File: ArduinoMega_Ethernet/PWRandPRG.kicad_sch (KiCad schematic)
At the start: 98 parts, among them J1 RJ45_Amphenol_RJMG1BD3B8K1ANR, J11 Micro_SD_Card_Det_Hirose_DM3AT, J7 EXT_3V3_I2C, J9 PROGRAM_POWER_USBC, U10 TXS0108EPW, U2 CH340C, U3 ISM330DHCX, U4 W5500, U5 AP63205WU, U6 AP63203WU, U7 SE050C2HQ1, U8 AP22804AW5, U9 MCP7940N-xST, Y2 25Mhz, Y3 32.768kHz

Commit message: w6100 manufacturing and project files
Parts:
- removed C36: 10uF, Capacitor_SMD:C_0805_2012Metric_Pad1.18x1.45mm_HandSolder, symbol Device:C_Small
- removed D3, D5: LED, LED_SMD:LED_0603_1608Metric, symbol Device:LED
- removed J1: RJ45_Amphenol_RJMG1BD3B8K1ANR, Connector_RJ:RJ45_Amphenol_RJMG1BD3B8K1ANR, symbol Connector:RJ45_Amphenol_RJMG1BD3B8K1ANR
- removed JP1: PMODE1, Jumper:SolderJumper-3_P1.3mm_Bridged12_Pad1.0x1.5mm, symbol Jumper:SolderJumper_3_Bridged12
- removed JP2: PMODE0, Jumper:SolderJumper-3_P1.3mm_Bridged12_Pad1.0x1.5mm, symbol Jumper:SolderJumper_3_Bridged12
- removed JP3: PMODE2, Jumper:SolderJumper-3_P1.3mm_Bridged12_Pad1.0x1.5mm, symbol Jumper:SolderJumper_3_Bridged12
- removed R17, R19: 330R, Resistor_SMD:R_0603_1608Metric, symbol Device:R_Small_US
- removed R21: 12.4k, Resistor_SMD:R_0603_1608Metric, symbol Device:R_Small_US
- removed R22: 10R, Resistor_SMD:R_0603_1608Metric, symbol Device:R_Small_US
- removed R24, R26: 82R, Resistor_SMD:R_0603_1608Metric, symbol Device:R_Small_US
- removed U4: W5500, Package_QFP:LQFP-48_7x7mm_P0.5mm, symbol Interface_Ethernet:W5500
- added C50: 100nF, Capacitor_SMD:C_0603_1608Metric, symbol Device:C_Small
- added FB3, FB4: FerriteBead_Small, Inductor_SMD:L_0603_1608Metric, symbol Device:FerriteBead_Small
- added IC1: W6100L, EXT_ETHERNET:QFP50P900X900X160-48N, symbol EXT_ETHERNET:W6100L
- added P1: RB1-125BAG1A, EXT_ETHERNET:WIZNET_RB1-125BAG1A, symbol EXT_ETHERNET:RB1-125BAG1A
- added R33: 12.3k, Resistor_SMD:R_0603_1608Metric, symbol Device:R_Small_US
- added R35, R36: 49.9R, Resistor_SMD:R_0603_1608Metric, symbol Device:R_Small_US
- C15, C16: value 6.8nF -> 100nF
- C17: value 22nF -> 100nF
- C19, C22: value 10nF -> 100nF
- C21: value 4.7uF -> 100nF; footprint Capacitor_SMD:C_0805_2012Metric_Pad1.18x1.45mm_HandSolder -> Capacitor_SMD:C_0603_1608Metric
- R18, R20: value 330R -> 470R
- R23, R25: value 49R -> 49.9R
- R27, R28, R29, R30: value 33R -> 3.3R
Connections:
- net +3V3: now also C15.1, C16.1, FB2.2, IC1.24 (3V3D_1), IC1.36 (3V3D_2); no longer C25.1, C26.1, C27.1, C29.1, C32.1, C34.1, FB2.1
- net ACT_LED: now also R18.1, IC1.20 (ACTN)
- net ETHERNET_CS: now also IC1.29 (CSN)
- net ETHERNET_MISO: now also IC1.33 (MISO)
- net ETHERNET_MOSI: now also IC1.32 (MOSI)
- net ETHERNET_SCLK: now also IC1.30 (SCLK)
- net ETHERNET_~{INT}: now also IC1.47 (INTN)
- net ETHERNET_~{RST}: now also IC1.48 (RSTN)
- net GND: now also C15.2, C16.2, C50.2, IC1.1 (GNDA_1), IC1.10 (GND_1), IC1.16 (GNDA_3), IC1.23 (GND_2), IC1.25 (MOD0), IC1.26 (MOD1), IC1.27 (MOD2), IC1.28 (MOD3), IC1.46 (GND_3), IC1.7 (GNDA_2), P1.L1, P1.L3, P1.S1 (Shield), P1.S2 (Shield), R33.2; no longer R18.1, R20.1
- net LINK_LED: now also R20.1, IC1.17 (LNKN)
- net at R30.2: now also R25.1, P1.R7 (RD+); no longer C15.1
- net at C30.2, R34.1, Y2.1: now also IC1.11 (XSCO)
- net at R20.2: now also P1.L4
- net at C19.1: now also R23.2, R25.2
- net at C28.2, R34.2, Y2.3: now also IC1.12 (XSCI)
- net 3V3_ANA: now reaches C22.1
- net 3V3_ANA: now also C21.1, FB2.1, IC1.15 (3V3A_2), IC1.8 (3V3A_1)
- net at R18.2: now also P1.L2
- net at R28.2: now also P1.R1 (TD+), R36.1; no longer R23.2
- net at R27.2: now also P1.R2 (TD-), R35.1; no longer R25.2
- net at C17.1: now also R35.2, R36.2
- net at R28.1: now also IC1.3 (TXOP)
- net at R29.2: now also R23.1, P1.R8 (RD-); no longer C16.1
- net at R27.1: now also IC1.2 (TXON)
- net at R29.1: now also IC1.5 (RXIN)
- net at R30.1: now also IC1.6 (RXIP)
- new net: IC1.9 (RSET_BG), R33.1
- new net +3.3VA: C50.1, P1.R3 (CT)
- new net 1V2_ANA: C25.1, FB4.1, IC1.4 (1V2A)
- new net 1V2_DIG: C26.1, C27.1, C29.1, C32.1, FB3.1, IC1.13 (1V2D_1), IC1.22 (1V2D_2), IC1.31 (1V2D_3), IC1.45 (1V2D_4)
- new net 1V2_OUT: C34.1, FB3.2, FB4.2, IC1.14 (1V2O)
- new net COL_LED: IC1.21 (COLN)
- new net DUP_LED: IC1.19 (DPXN)
- new net SPEED_LED: IC1.18 (SPDN)
- no-connect marks 13 -> 25
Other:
- note added: "Dual Stack Ethernet <-> SPI"
- note removed: "SPI Ethernet Controller ->SPI"
- moved on the sheet: C17, C19, C25, C26, C27, C28, C29, C30, C32, C34, FB2, R18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

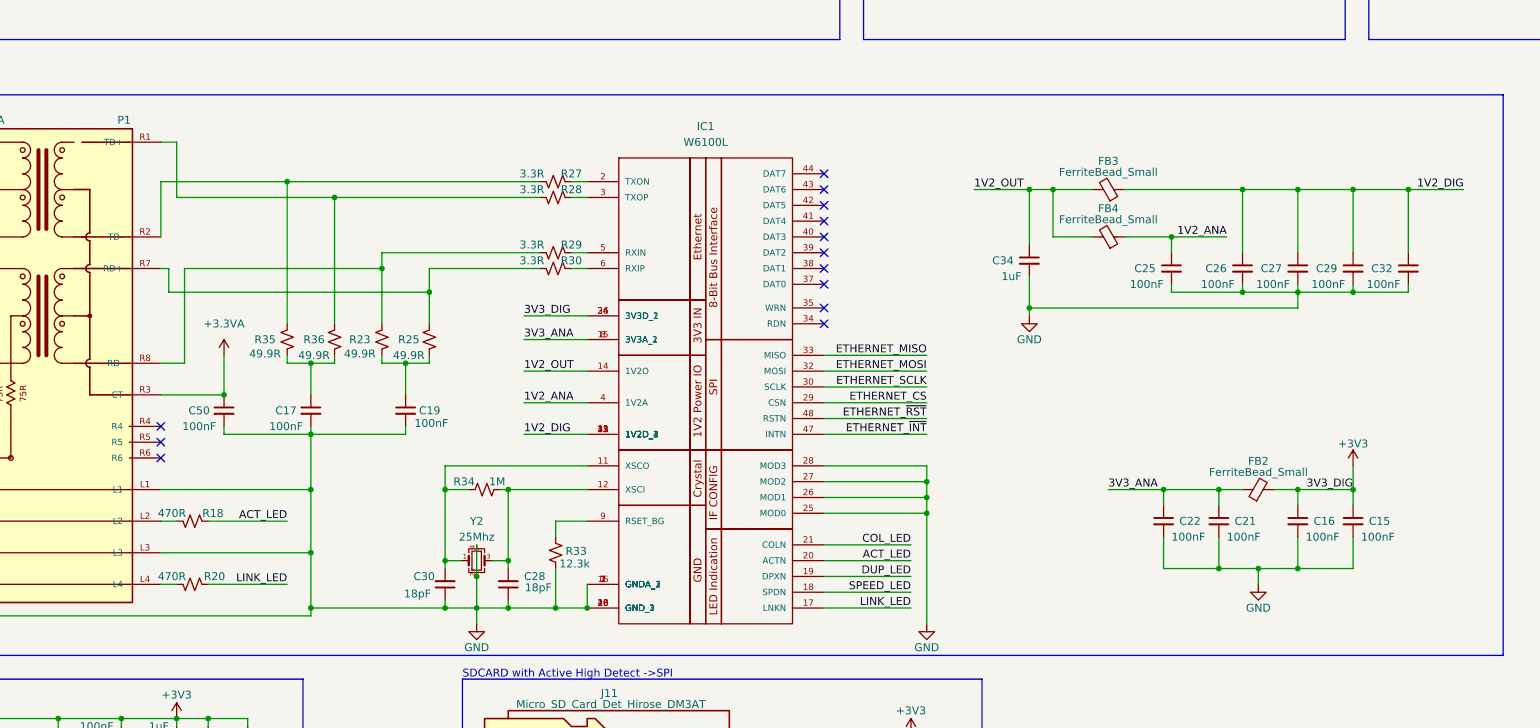
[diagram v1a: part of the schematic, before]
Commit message: bom and component sizing
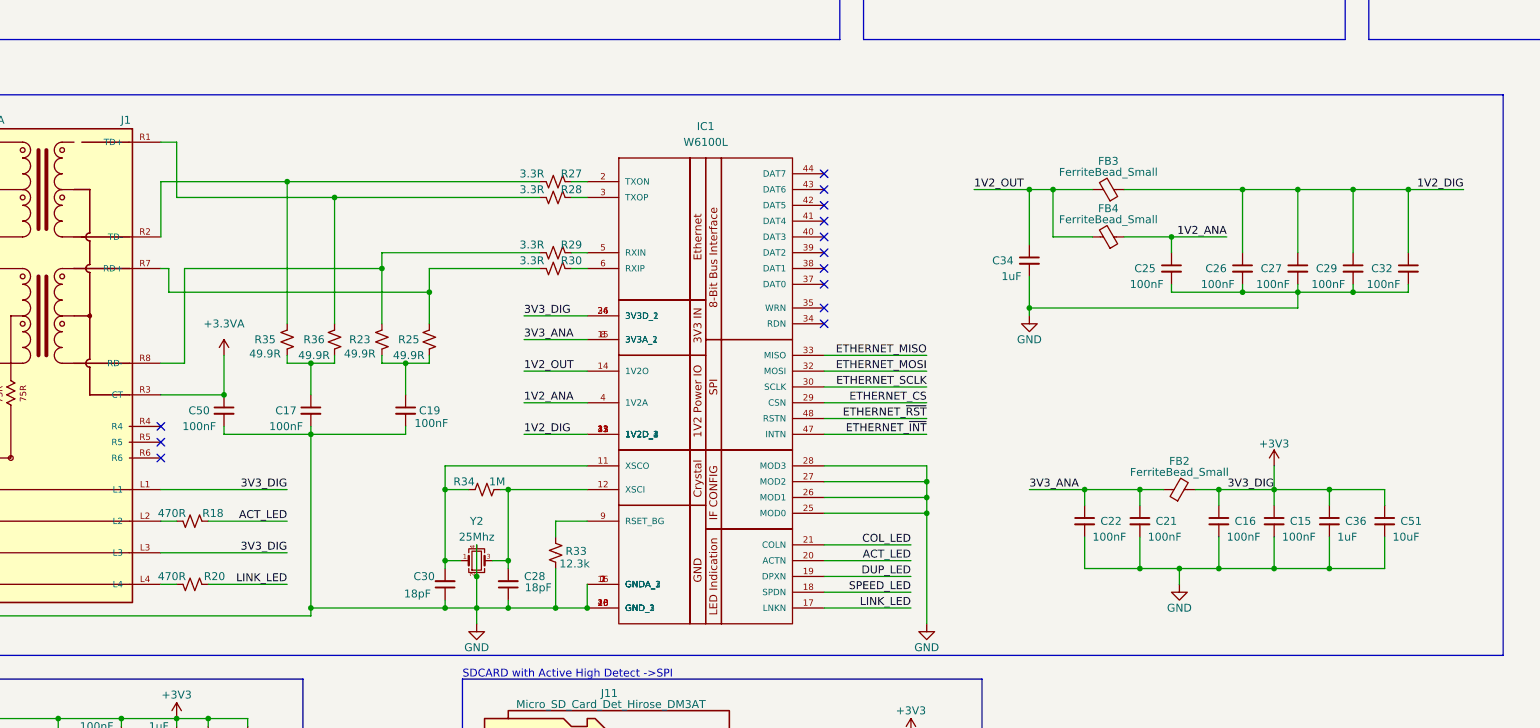
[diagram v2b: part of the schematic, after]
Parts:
- added C36: 1uF, Capacitor_SMD:C_0603_1608Metric, symbol Device:C_Small
- added C51: 10uF, Capacitor_SMD:C_0805_2012Metric_Pad1.18x1.45mm_HandSolder, symbol Device:C_Small
- renumbered P1 to J1
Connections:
- net +3V3: now also J1.L1, J1.L3, C36.1, C51.1
- net GND: now also C36.2, C51.2; no longer J1.L1, J1.L3
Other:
- moved on the sheet: C15, C16, C21, C22, FB2
